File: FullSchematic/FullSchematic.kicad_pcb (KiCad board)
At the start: 4 copper layers, 154.6 x 135.2 mm, 100 parts, among them J1 USB_A, J10 LCD_Conn, J2 ATX-24, J3 Red Banana Jack, J4 Black Banana Jack, J5 2x6 Pin Header, J6 2x6 Pin Header, J7 CT3151-2, J8 CT3151-2, J9 2x6 Pin Header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

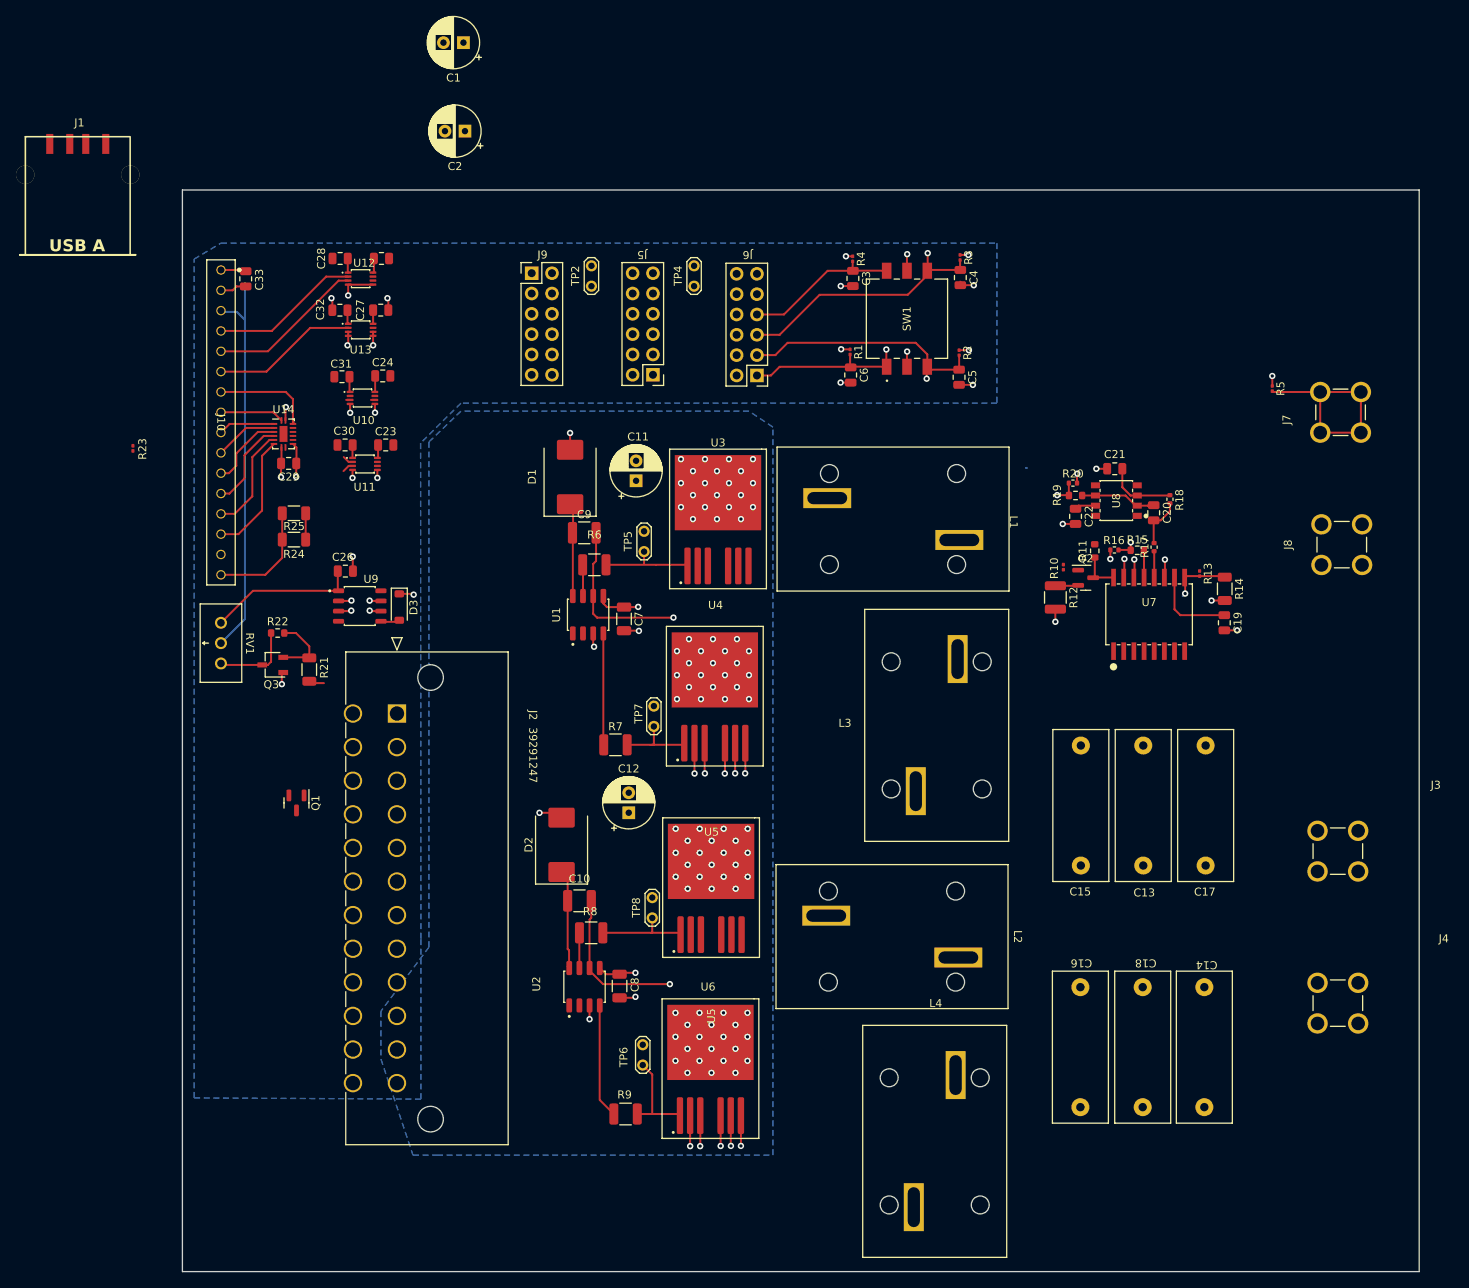
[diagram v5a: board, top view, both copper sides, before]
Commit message: Routed all connections, need constraints
all the connections have been made. The JLCPCB constraints must be entered, but likely will not be a problem.

Will need to tidy up all connections/spacing/etc.
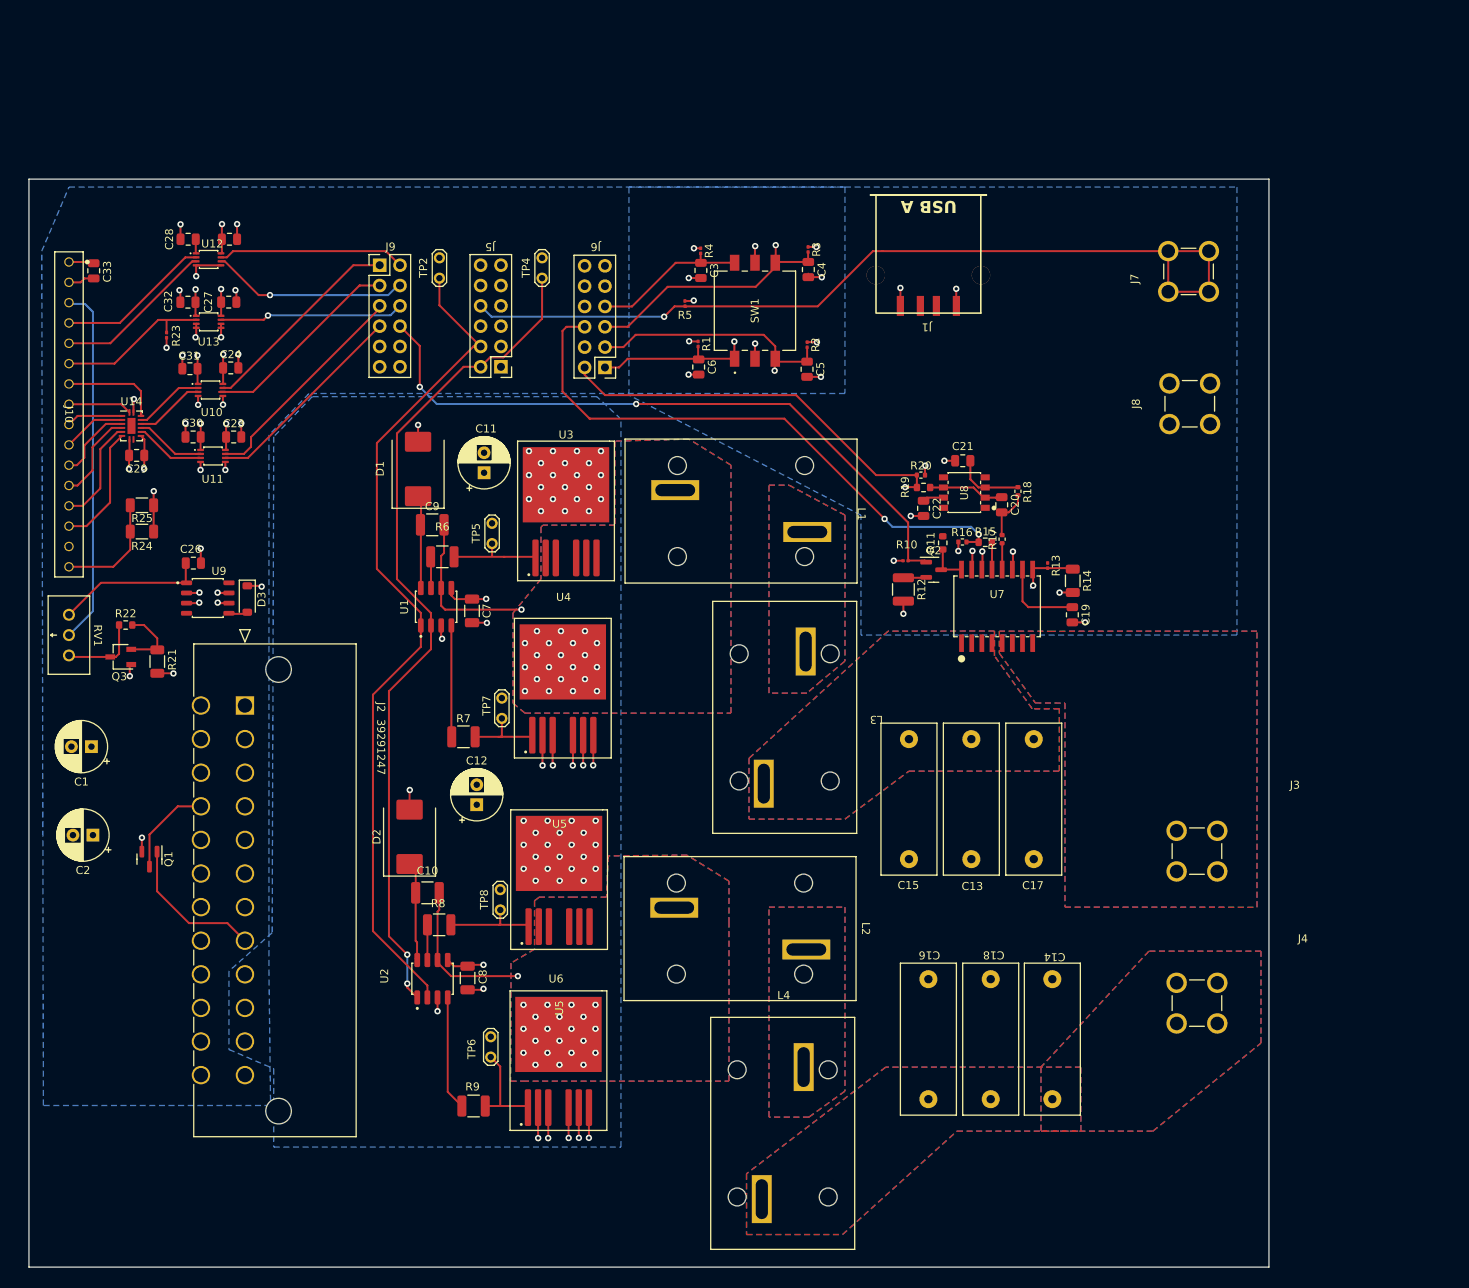
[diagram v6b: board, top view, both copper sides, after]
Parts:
- moved J1 106.6 mm to (172.4, 26.0), turned to 180 degrees
- moved C1 99.5 mm to (67.8, 94.9)
- moved C2 99.5 mm to (68.0, 106.0)
- moved R5 74.2 mm to (142.0, 39.6)
- moved J7 25.9 mm to (205.0, 35.5)
- moved J8 25.9 mm to (205.1, 52.1)
- moved C13 21.5 mm to (177.8, 101.5)
- moved C15 21.5 mm to (170.0, 101.5)
- moved C17 21.5 mm to (185.6, 101.5)
- moved R10 19.7 mm to (169.6, 71.7), turned to 0 degrees
- moved Q1 19.7 mm to (75.1, 109.0)
- moved C25 19.2 mm to (85.1, 31.5)
- moved C28 19.2 mm to (79.9, 31.5)
- moved U12 19.2 mm to (82.5, 34.0)
- moved C12 19.0 mm to (116.0, 102.2)
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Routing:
- net NON_INV: track 0.61 -> 106.1 mm
- net INV: track 0.40 -> 105.4 mm, vias 0 -> 2
- net RELAY_TRIP_N: track 26.4 -> 110.4 mm, vias 0 -> 1
- net OC_RESET_N: track 0.48 -> 83.9 mm, vias 0 -> 2
- net C_REF: track 2.53 -> 72.6 mm, vias 1 -> 2
- net C_SENSE: track 3.05 -> 50.7 mm
- net *OE: track 0.00 -> 28.5 mm
- net SRCLK: track 0.24 -> 26.8 mm
- net SER: track 0.00 -> 26.1 mm
- net RCLK: track 0.49 -> 25.6 mm
- net Net-(U12-B2): track 0.00 -> 24.6 mm, vias 0 -> 1
- net Net-(U12-B1): track 0.00 -> 23.4 mm
- net Net-(U13-B1): track 0.00 -> 23.1 mm, vias 0 -> 1
- net PWR_OK: track 0.00 -> 18.5 mm
- net COM: track 103.5 -> 119.5 mm, vias 43 -> 53
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- added copper zone on In2.Cu, net +3.3V
- added copper zone on B.Cu, net AMP_OUT
- added copper zone on F.Cu, net AMP_OUT
- added copper zone on In2.Cu, net AMP_OUT
- added copper zone on In1.Cu, net COM
- added copper zone on B.Cu, net Net-(L1-Pad2)
- added copper zone on F.Cu, net Net-(L1-Pad2)
- added copper zone on In2.Cu, net Net-(L1-Pad2)
- added copper zone on B.Cu, net Net-(L2-Pad2)
- added copper zone on F.Cu, net Net-(L2-Pad2)
- added copper zone on In2.Cu, net Net-(L2-Pad2)
- added copper zone on B.Cu, net Net-(U1-VS)
- added copper zone on F.Cu, net Net-(U1-VS)
- added copper zone on In2.Cu, net Net-(U1-VS)
- added copper zone on B.Cu, net Net-(U2-VS)
- added copper zone on F.Cu, net Net-(U2-VS)
- added copper zone on In2.Cu, net Net-(U2-VS)
- added copper zone on B.Cu, net OCTA_IN
- added copper zone on F.Cu, net OCTA_IN
- added copper zone on In2.Cu, net OCTA_IN
- added copper zone on B.Cu, net OCTA_OUT
- added copper zone on F.Cu, net OCTA_OUT
- added copper zone on In2.Cu, net OCTA_OUT
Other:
- board size 154.6 x 135.2 mm -> 155 x 136 mm

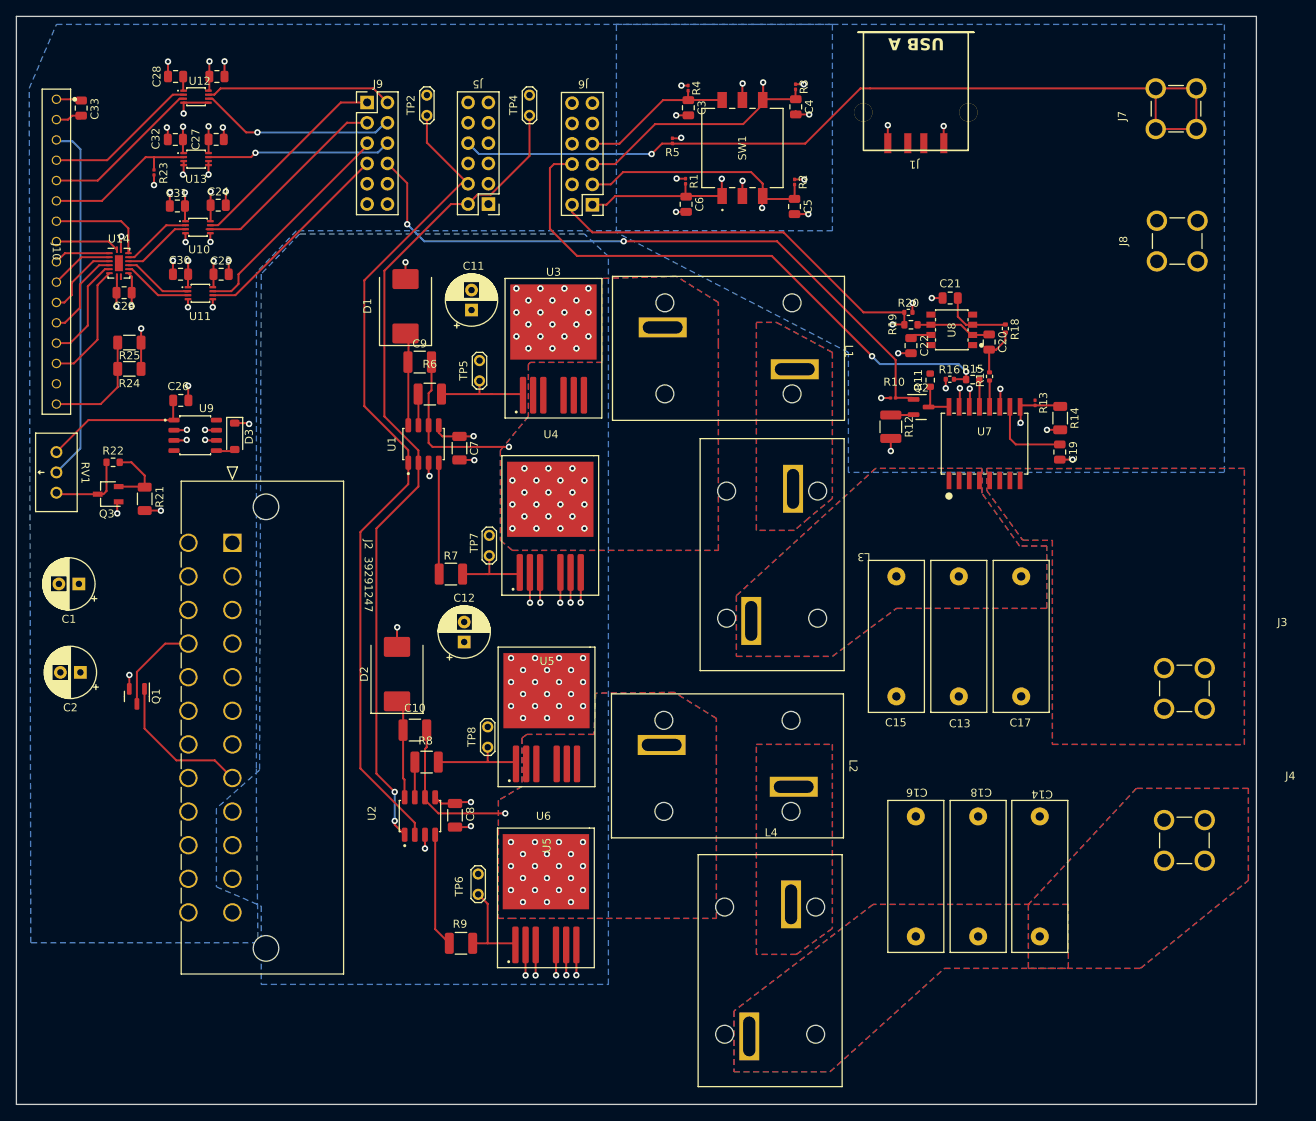
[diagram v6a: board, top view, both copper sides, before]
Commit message: PCB V.2
Fixed all DRC errors, tidied everything up.
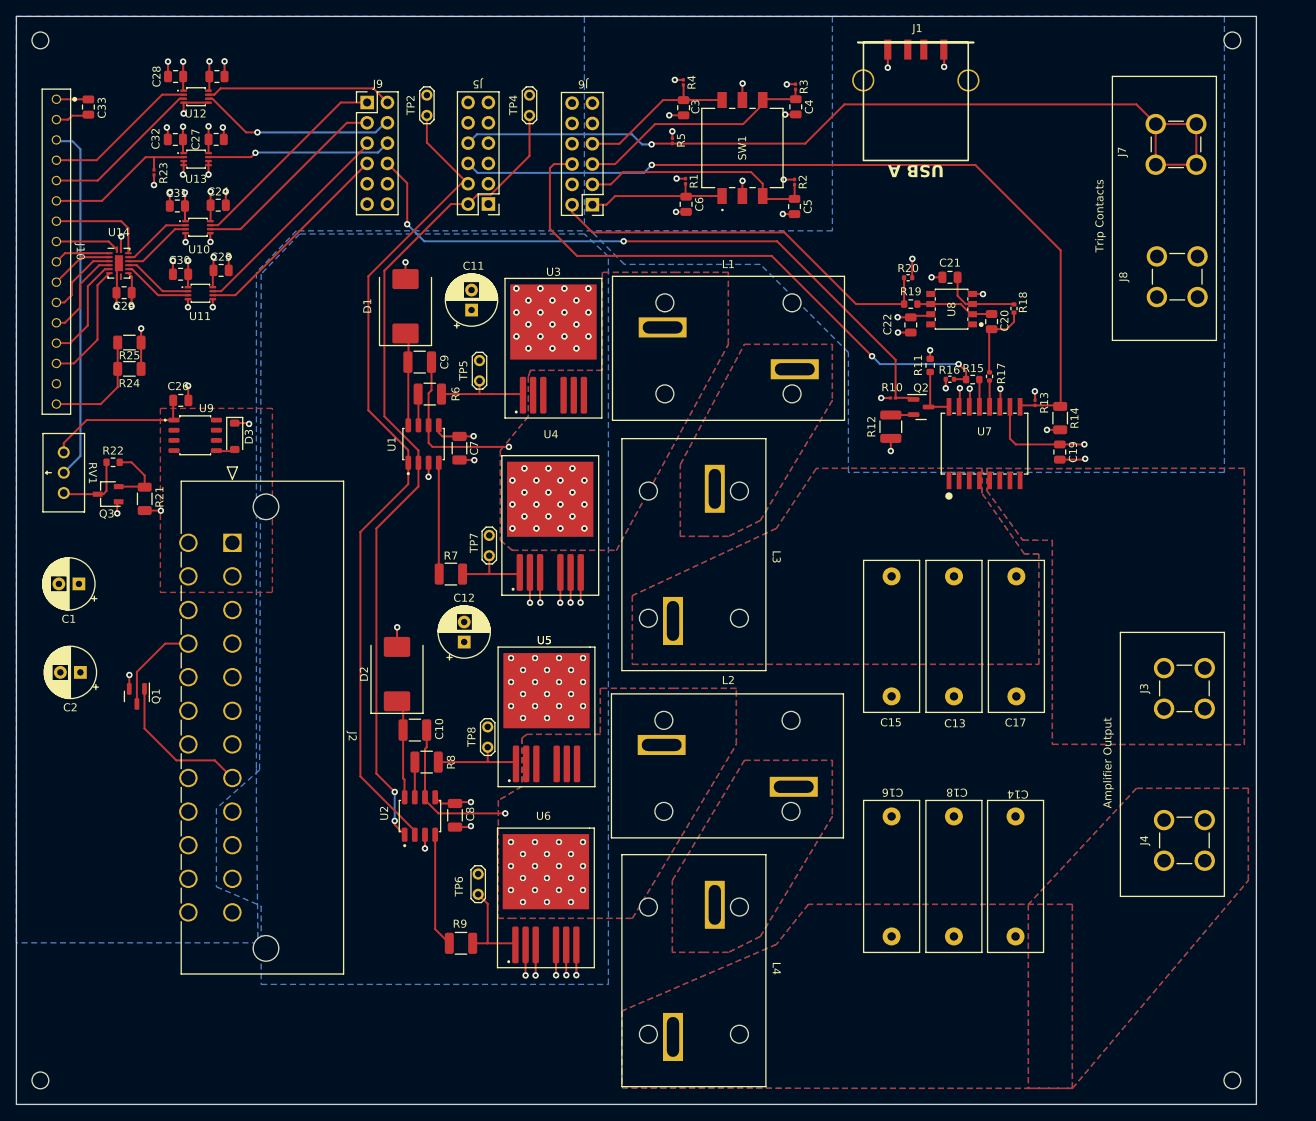
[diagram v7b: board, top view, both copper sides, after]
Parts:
- added REF**: MountingHole_2.1mm, MountingHole:MountingHole_2.1mm, F.Cu at (212.0, 27.0)
- added REF**: MountingHole_2.1mm, MountingHole:MountingHole_2.1mm, F.Cu at (63.0, 27.0)
- added REF**: MountingHole_2.1mm, MountingHole:MountingHole_2.1mm, F.Cu at (212.0, 157.0)
- added REF**: MountingHole_2.1mm, MountingHole:MountingHole_2.1mm, F.Cu at (63.0, 157.0)
- moved J1 16.0 mm to (172.4, 42.0), turned to 0 degrees
- moved L3 9.78 mm to (144.7, 91.3)
- moved L4 9.53 mm to (144.7, 143.3), turned to -90 degrees
- moved J7 4.46 mm to (205.0, 40.0)
- moved J8 4.46 mm to (205.1, 56.5)
- moved R20 4.33 mm to (171.5, 56.7)
- moved C14 3.03 mm to (184.9, 131.5)
- moved C16 3.03 mm to (169.4, 131.5)
- moved C18 3.03 mm to (177.2, 131.5)
- moved R18 2.73 mm to (184.7, 60.5)
- moved C21 2.59 mm to (176.7, 56.6)
- moved C22 2.59 mm to (171.8, 62.6)
- moved R19 2.59 mm to (171.8, 60.0)
- moved U8 2.59 mm to (176.9, 60.4)
- moved C20 2.57 mm to (181.9, 62.1)
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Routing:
- net FAULT_N: track 7.59 -> 104.1 mm
- net +5V: track 44.0 -> 52.3 mm, vias 8 -> 13
- net -12V: track 6.04 -> 0.00 mm, vias 4 -> 0
- net +12V: track 20.0 -> 14.9 mm
- net Net-(C20-Pad2): track 6.36 -> 9.90 mm
- net COM: track 119.5 -> 122.5 mm, vias 53 -> 54
- net Net-(SW1-2): track 33.2 -> 30.5 mm, vias 1 -> 0
- net Net-(C6-Pad1): track 20.6 -> 18.5 mm, vias 1 -> 0
- net Net-(SW1-4): track 31.5 -> 29.5 mm, vias 1 -> 0
- net V_OC: track 5.21 -> 7.06 mm
- net *OE: track 28.5 -> 26.8 mm
- net Net-(Q3-E): track 10.3 -> 9.16 mm
- net Net-(U8-+IN): track 8.71 -> 9.81 mm
- net NON_INV: track 106.1 -> 105.1 mm
- net SRCLK: track 26.8 -> 26.0 mm
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- added copper zone on F.Cu, net -12V
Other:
- board text added: "Amplifier Output"
- board text added: "Trip Contacts"
